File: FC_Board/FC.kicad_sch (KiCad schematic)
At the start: 82 parts, among them J1 Programmer_pins, J2 Pyro1, J3 Pyro2, J4 Pyro3, J5 Pyro4, J8 MEM2090-00-145-00-A_REVA, M1 Motor_Servo, M2 Motor_Servo, M3 Motor_Servo, M4 Motor_Servo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

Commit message: Schematic update
- Add: GPS USB and UART
- Add: USB 2.0 standard related circuitry
- Finished third SPI Bus
- Started Quad SPI Bus for data logging (SD card and Flash)
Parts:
- added BT2: Backup Bat 3.7V, Connector_JST:JST_EH_B2B-EH-A_1x02_P2.50mm_Vertical, symbol Device:Battery_Cell
- added C31, C33: 2.2uF, symbol Device:C
- added J7: USB_B_Micro, Connector_USB:USB_Micro-B_Molex-105017-0001, symbol Connector:USB_B_Micro
- added R10, R9: 27, symbol Device:R
- added R22: 100k, symbol Device:R
- added U10: ADPL44002AUJZ-5.0-R7, Package_TO_SOT_SMD:TSOT-23-5, symbol Regulator_Linear:ADP7142AUJZ-5.0
- added U11: USBLC6-2SC6, Package_TO_SOT_SMD:SOT-23-6, symbol Power_Protection:USBLC6-2SC6
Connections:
- net 3V3: no longer U7.22 (V_BCKP)
- net FLASH_EN: now also U1.57 (EBIRDY3/RPF2/SDA3/RF2)
- net GND: now also BT2.2 (-), C31.2, C33.1, J7.5 (GND), J7.6 (Shield), R22.2, U10.2 (GND), U11.2 (GND)
- net GPS_CS: now also U1.9 (EBIOE/AN19/RPC4/PMRD/RC4)
- net GPS_INT: now also U1.61 (EBIA14/PMCS1/PMA14/RA4)
- net GPS_RESET: now also U1.80 (EBID13/ETXD3/PMD13/RD13)
- net IMU_INT1: now also U1.5 (EBID7/AN15/PMD7/RE7); no longer U1.100 (EBID4/AN18/PMD4/RE4)
- net IMU_INT2: now also U1.4 (EBID6/AN16/PMD6/RE6); no longer U1.99 (EBID3/RPE3/PMD3/RE3)
- net MAG_DR: now also U1.1 (AN23/AERXERR/RG15); no longer U1.96 (TRD1/SQID1/RG12)
- net MAG_INT: now also U1.2 (EBIA5/AN34/PMA5/RA5); no longer U1.97 (TRD0/SQID0/RG13)
- net SPI3_CLK: now reaches U1.43 (EBIA1/AN9/ERXD2/AETXD3/RPB14/SCK3/PMA1/RB14)
- net SPI3_MISO: now reaches U1.47 (AN32/AETXD0/RPD14/RD14)
- net SPI3_MOSI: now reaches U1.48 (AN33/AETXD1/RPD15/SCK6/RD15)
- net at U7.5 (USB_DM): now also R10.2
- net at U7.6 (USB_DP): now also R9.2
- net VDD_USB: now reaches U7.7 (VDD_USB)
- net VDD_USB: now also C31.1, R22.1, U10.4 (SENSE/ADJ), U10.5 (VOUT)
- new net: C33.2, J7.1 (VBUS), U10.1 (VIN), U10.3 (EN), U11.5 (VBUS)
- new net: J7.2 (D-), U11.3 (I/O2)
- new net: J7.3 (D+), U11.1 (I/O1)
- new net: R9.1, U11.6 (I/O1)
- new net: R10.1, U11.4 (I/O2)
- new net V_BACKUP: BT2.1 (+), U7.22 (V_BCKP)
- no-connect marks 1 -> 4
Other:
- note added: "ESD-protection (USB2.0 standard)"
- note added: "SPI1 - MAG & IMU SPI2 - ALT/TEMP (recommended) SPI3 - GPS SPI4 - LOGGING"
- note added: "SPI3 CLK"
- note added: "SPI3 MISO"
- note added: "SPI3 MOSI"
- note added: "SPI4 CLK"
- note added: "SPI4 SIO0"
- note added: "SPI4 SIO1"
- note added: "SPI4 SIO2"
- note added: "SPI4 SIO3"
- note removed: "Adicionar interface leitura. USB maybe? Bué bulky idk..."
- note removed: "Ligar USB para dar debug ao GPS?"
- note removed: "SPI separado também. Partilhado apenas com logging"
- note removed: "SPI1 - MAG & IMU SPI2 - ALT/TEMP (sensitive/recommended) SPI3 - GPS & LOGGING"
- moved on the sheet: BT1, C11, C12, C13, C18, C19, C20, C21, C29, C3, C4, C8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

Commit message: Schematic Done
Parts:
- removed C24: 1uF, symbol Device:C_Polarized
- removed R8: 0.04, symbol Device:R_Shunt
- added C24: 1uF, Capacitor_SMD:C_0603_1608Metric_Pad1.08x0.95mm_HandSolder, symbol Device:C
- added J6: Conn_01x05, Connector_PinHeader_2.54mm:PinHeader_1x05_P2.54mm_Vertical, symbol Connector_Generic:Conn_01x05
- added R23, R24, R25, R26, R27, R28: 10k, Resistor_SMD:R_0805_2012Metric_Pad1.20x1.40mm_HandSolder, symbol Device:R
- added R29: 0.04, Resistor_SMD:R_2512_6332Metric_Pad1.40x3.35mm_HandSolder, symbol Device:R
- AE1: footprint (none) -> Connector_Coaxial:SMA_Samtec_SMA-J-P-H-ST-EM1_EdgeMount
- BT1: footprint (none) -> Connector_AMASS:AMASS_XT60IPW-M_1x03_P7.20mm_Horizontal
- BZ1: footprint (none) -> Buzzer_Beeper:Buzzer_12x9.5RM7.6; Mouser link (none) -> https://pt.mouser.com/ProductDetail/Same-Sky/CMT-1295-85T?q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
- C10, C11, C12, C13, C14, C15, C16, C9: footprint (none) -> Capacitor_SMD:C_1210_3225Metric_Pad1.33x2.70mm_HandSolder; Mouser link (none) -> https://pt.mouser.com/ProductDetail/TAIYO-YUDEN/MSASE32MSB5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
- C18: value 0.22uF -> 1uF; footprint (none) -> Capacitor_SMD:C_0603_1608Metric_Pad1.08x0.95mm_HandSolder; Mouser link (none) -> https://pt.mouser.com/ProductDetail/TAIYO-YUDEN/MLASU168SB5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
- C20: footprint (none) -> Capacitor_SMD:C_0603_1608Metric_Pad1.08x0.95mm_HandSolder; Mouser link (none) -> https://pt.mouser.com/ProductDetail/TAIYO-YUDEN/MLASU168SB5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
- C21: footprint (none) -> Capacitor_SMD:C_0805_2012Metric_Pad1.18x1.45mm_HandSolder; Mouser link (none) -> https://pt.mouser.com/ProductDetail/Murata-Electronics/GCM2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
- C31, C33: footprint (none) -> Capacitor_SMD:C_0603_1608Metric_Pad1.08x0.95mm_HandSolder; Mouser link (none) -> https://pt.mouser.com/ProductDetail/TAIYO-YUDEN/MLASE168BB7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
- D1: footprint (none) -> Diode_SMD:D_SOD-323_HandSoldering
- D2, D3: footprint (none) -> LED_THT:LED_D3.0mm
- F1: footprint (none) -> Fuse:Fuseholder_Cylinder-5x20mm_Schurter_0031_8201_Horizontal_Open; Mouser link (none) -> https://pt.mouser.com/ProductDetail/Schurter/0031.8201.G?qs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
- J1: footprint (none) -> Connector_PinHeader_2.54mm:PinHeader_1x06_P2.54mm_Horizontal
- J2, J3, J4, J5: footprint (none) -> Connector_Molex:Molex_KK-254_AE-6410-02A_1x02_P2.54mm_Vertical
- M1, M2, M3, M4: footprint (none) -> Connector_Molex:Molex_KK-254_AE-6410-03A_1x03_P2.54mm_Vertical
- Q1: footprint (none) -> Package_TO_SOT_SMD:SOT-23-3; Mouser link (none) -> https://pt.mouser.com/ProductDetail/Infineon-Technologies/B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
- Q2, Q3, Q4, Q5, Q6: footprint (none) -> Package_TO_SOT_SMD:SOT-23; Mouser link (none) -> https://pt.mouser.com/ProductDetail/Vishay-Siliconix/SQ2318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
- R10, R9: footprint (none) -> Resistor_SMD:R_0603_1608Metric_Pad0.98x0.95mm_HandSolder; Mouser link (none) -> https://pt.mouser.com/ProductDetail/Panasonic/ERJ-3RED27R0V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
- R11, R7: footprint (none) -> Resistor_SMD:R_0603_1608Metric_Pad0.98x0.95mm_HandSolder; Mouser link (none) -> https://pt.mouser.com/ProductDetail/SEI-Stackpole/RNCE0603B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
- R2: footprint (none) -> Resistor_SMD:R_0805_2012Metric_Pad1.20x1.40mm_HandSolder; Mouser link (none) -> https://pt.mouser.com/ProductDetail/Vishay/TNPW08051K00FEEA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
- R22, R3: footprint (none) -> Resistor_SMD:R_1206_3216Metric_Pad1.30x1.75mm_HandSolder; Mouser link (none) -> https://pt.mouser.com/ProductDetail/Bourns/CHV1206-JW-104EL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
- R4: footprint (none) -> Resistor_SMD:R_0805_2012Metric_Pad1.20x1.40mm_HandSolder
- U1: footprint TQFP100_PF_MCH -> QFP50P1600X1600X120-100N
- U2: footprint Package_TO_SOT_THT:TO-220-3_Vertical -> Package_TO_SOT_THT:TO-220-3_Horizontal_TabDown
- U4: footprint LSM6DS3TR-C:LGA-14-2.5X3MM -> LGA-14-2.5X3MM
- U5: footprint LIS3MDLTR:XDCR_LIS3MDLTR -> XDCR_LIS3MDLTR
- U8: footprint SOIJ8_SM_MCH -> Package_SO:SOIC-8W_5.3x5.3mm_P1.27mm; Mouser link (none) -> https://br.mouser.com/ProductDetail/Microchip-Technology/SS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
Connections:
- net 3V3: now also R4.1, C24.2, R23.2, R24.2, R25.2, R26.2, R27.2, R28.2; no longer R4.2
- net ALT_CS: now also R4.2; no longer R4.1
- net FLASH_CLK: now also J6.4 (Pin_4)
- net FLASH_EN: now also J6.1 (Pin_1)
- net GND: now also C20.2, C21.2, U3.1 (GND), C24.1, J6.5 (Pin_5)
- net Pyro1: now also U1.88 (EBID8/RPG0/PMD8/RG0); no longer U1.82 (SQICS1/RPD5/RD5)
- net SD_CMD: now also U1.82 (SQICS1/RPD5/RD5)
- net SD_D0: now also R27.1
- net SD_D1: now also R28.1
- net SD_D2: now also R25.1
- net SD_D3: now also R26.1
- net SD_IN#: now also U1.41 (EBIA11/AN7/ERXD0/AECRS/PMA11/RB12)
- net Shunt_IN: now also U9.8 (IN+), R29.1
- net Shunt_OUT: now also U9.7 (IN-), R29.2
- net FLASH_SO: now reaches U8.2 (SO/SIO1)
- net FLASH_SO: now also J6.2 (Pin_2)
- net at U8.3 (WP#/SIO2): now also R24.1
- net FLASH_SI: now reaches U8.5 (SI/SIO0)
- net FLASH_SI: now also J6.3 (Pin_3)
- net at U8.7 (HOLD/SIO3): now also R23.1
- net SPI4_CLK: now reaches U1.89 (TRCLK/SQICLK/RA6)
- net SPI4_SIO3: now reaches U1.90 (TRD3/SQID3/RA7)
- net SPI4_SIO2: now reaches U1.95 (TRD2/SQID2/RG14)
- net SPI4_SIO1: now reaches U1.96 (TRD1/SQID1/RG12)
- net SPI4_SIO0: now reaches U1.97 (TRD0/SQID0/RG13)
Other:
- note added: "Conector para leitura externa"
- note added: "FLASH DATA LOGGING"
- note added: "SPI1 - MAG & IMU SPI2 - ALT/TEMP (recommended) SPI3 - GPS & FLASH SPI4 - SD CARD"
- note added: "Zener dá clamp para cumprir máx vgs quando reverse polarity. Para o PMOS que escolhi não é necessário."
- note removed: "Como é que este CMD funciona? Sequer preciso em modo SPI?"
- note removed: "GPS FLASH DATA LOGGING"
- note removed: "SPI1 - MAG & IMU SPI2 - ALT/TEMP (recommended) SPI3 - GPS SPI4 - LOGGING"
- note removed: "Zener dá clamp para cumprir máx vgs quando reverse polarity"
- moved on the sheet: C21, U3

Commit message: Started PCB
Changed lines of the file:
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@@
-	)
-	(junction
-		(at 208.28 102.87)
-		(diameter 0)
-		(color 0 0 0 0)
 	)
 	(junction
@@
 	(junction
 		(at 262.89 256.54)
-		(diameter 0)
-		(color 0 0 0 0)
-	)
-	(junction
-		(at 208.28 67.31)
 		(diameter 0)
 		(color 0 0 0 0)
@@
 		)
 		(stroke
-			(width 0)
-			(type default)
-		)
-	)
-	(wire
-		(pts
-			(xy 208.28 67.31) (xy 208.28 102.87)
-		)
-		(stroke

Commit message: First placement attempt
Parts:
- BT1: footprint Connector_AMASS:AMASS_XT60IPW-M_1x03_P7.20mm_Horizontal -> Connector_AMASS:AMASS_XT60-M_1x02_P7.20mm_Vertical
- U2: footprint Package_TO_SOT_THT:TO-220-3_Horizontal_TabDown -> Package_TO_SOT_THT:TO-220-3_Vertical
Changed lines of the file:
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@@
 			)
 		)
-		(property "Footprint" "Package_TO_SOT_THT:TO-220-3_Horizontal_TabDown"
+		(property "Footprint" "Package_TO_SOT_THT:TO-220-3_Vertical"
 			(at 91.44 50.165 0)
 			(effects
@@
 			)
 		)
-		(property "Footprint" "Connector_AMASS:AMASS_XT60IPW-M_1x03_P7.20mm_Horizontal"
+		(property "Footprint" "Connector_AMASS:AMASS_XT60-M_1x02_P7.20mm_Vertical"
 			(at 30.48 63.246 90)
 			(effects

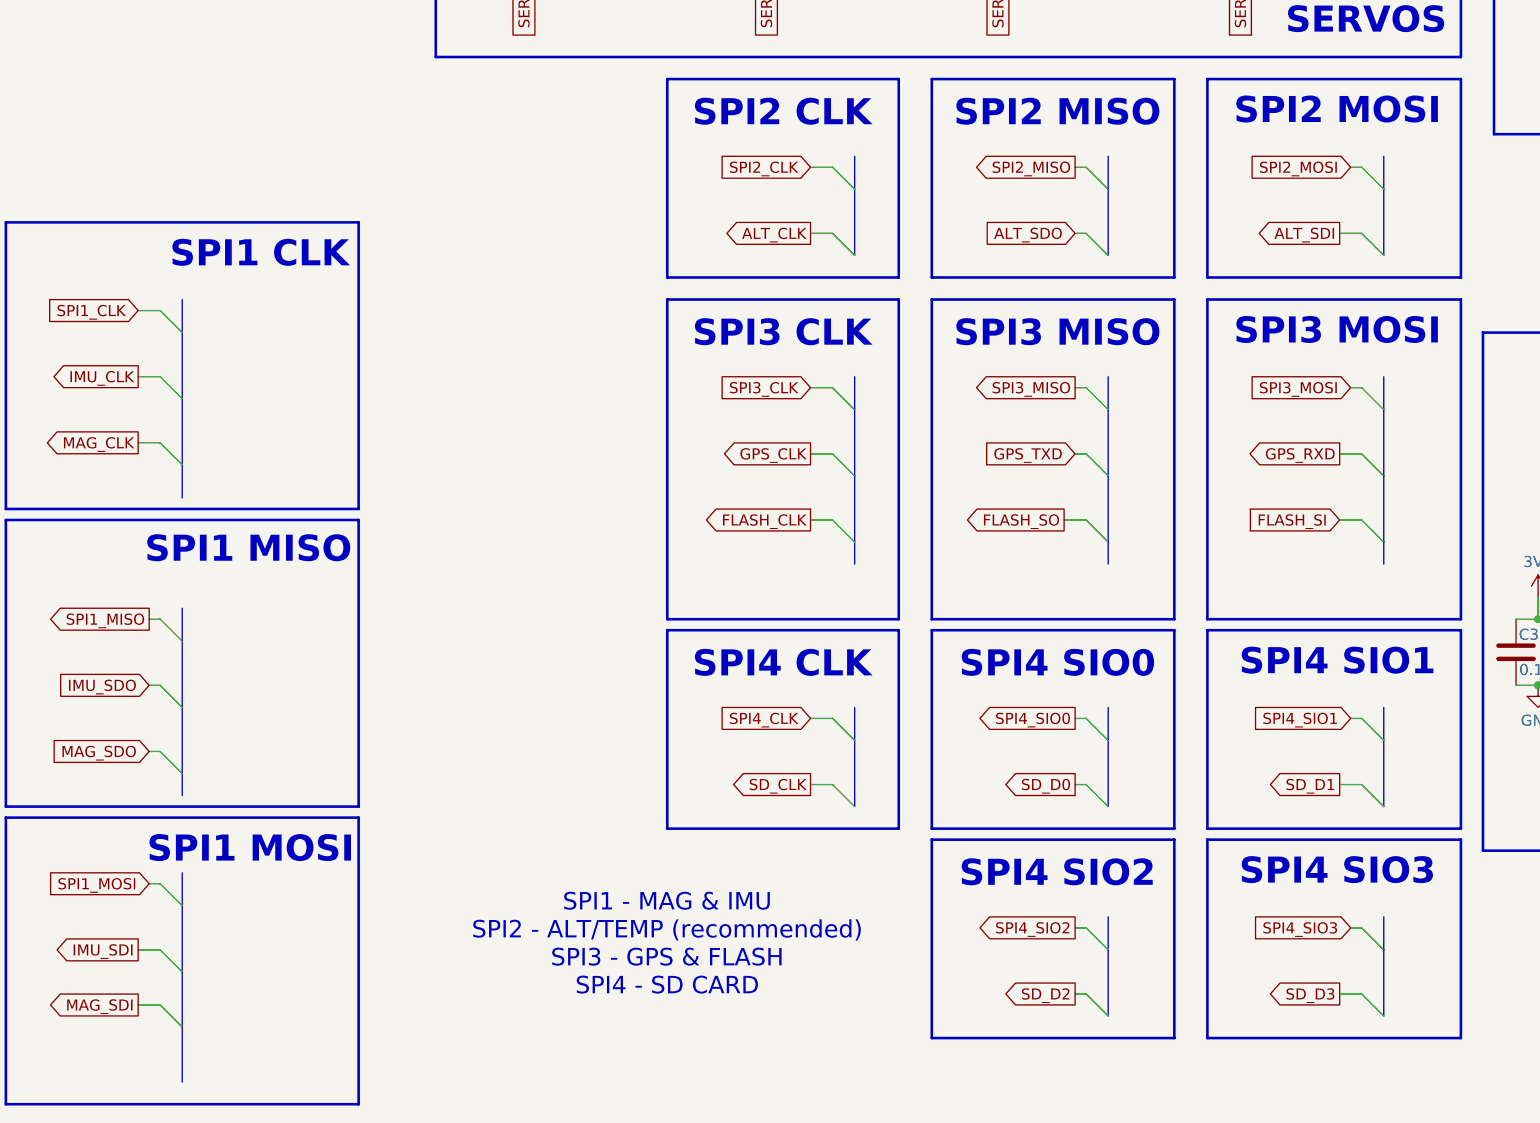
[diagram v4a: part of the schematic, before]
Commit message: Transitioning to 4 layers
Tried 2 layer routing to minimize cost. Too many tracks...
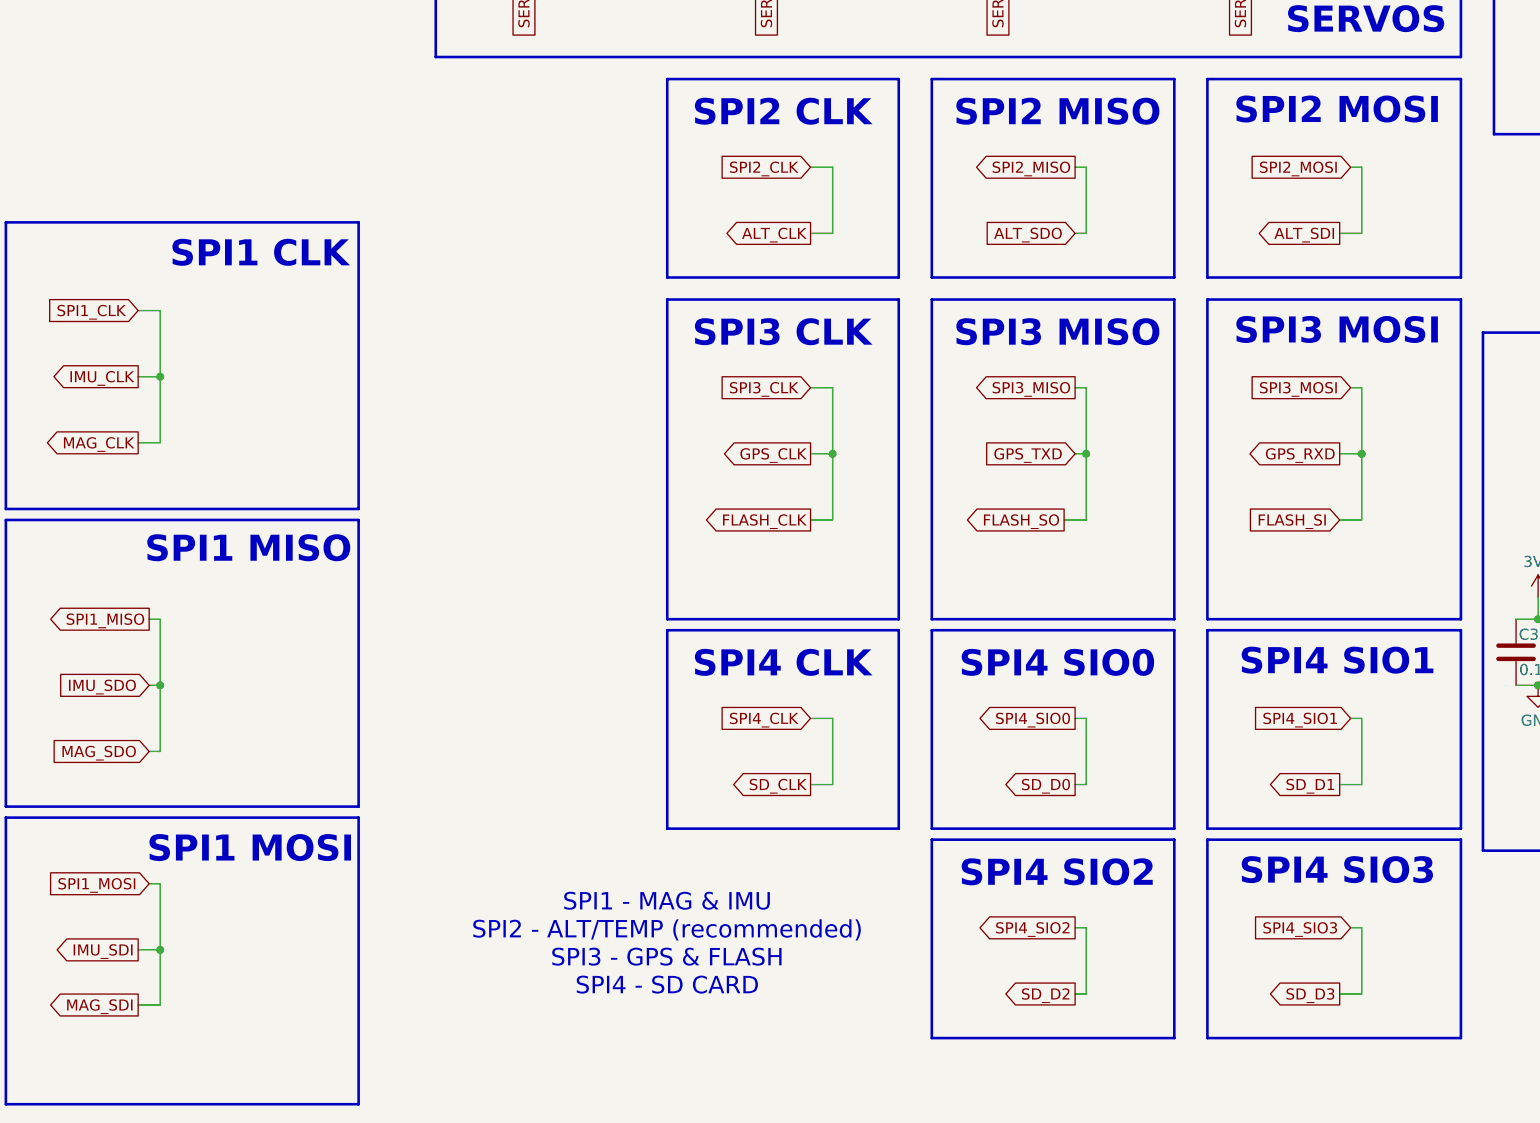
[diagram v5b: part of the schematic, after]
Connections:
- net GPS_CLK is gone; now on net FLASH_CLK: U7.19 (SCL/SPI_CLK)
- net GPS_RXD is gone; now on net FLASH_SI: U7.21 (RXD/SPI_MOSI)
- net GPS_TXD is gone; now on net FLASH_SO: U7.20 (TXD/SPI_MISO)
- net MAG_CLK is gone; now on net IMU_CLK: U5.1 (SCL/SPC)
- net MAG_SDI is gone; now on net IMU_SDI: U5.11 (SDA/SDI/SDO)
- net MAG_SDO is gone; now on net IMU_SDO: U5.9 (SDO/SA1)
- net SPI1_CLK is gone; now on net IMU_CLK: U1.76 (RPD1/SCK1/RD1)
- net SPI1_MISO is gone; now on net IMU_SDO: U1.73 (SOSCO/RPC14/T1CK/RC14)
- net SPI1_MOSI is gone; now on net IMU_SDI: U1.72 (SOSCI/RPC13/RC13)
- net SPI2_CLK is gone; now on net ALT_CLK: U1.10 (AN14/C1IND/ECOL/RPG6/SCK2/RG6)
- net SPI2_MISO is gone; now on net ALT_SDO: U1.6 (EBIA6/AN22/RPC1/PMA6/RC1)
- net SPI2_MOSI is gone; now on net ALT_SDI: U1.7 (EBIA12/AN21/RPC2/PMA12/RC2)
- net SPI3_CLK is gone; now on net FLASH_CLK: U1.43 (EBIA1/AN9/ERXD2/AETXD3/RPB14/SCK3/PMA1/RB14)
- net SPI3_MISO is gone; now on net FLASH_SO: U1.47 (AN32/AETXD0/RPD14/RD14)
- net SPI3_MOSI is gone; now on net FLASH_SI: U1.48 (AN33/AETXD1/RPD15/SCK6/RD15)
- net SPI4_CLK is gone; now on net SD_CLK: U1.89 (TRCLK/SQICLK/RA6)
- net SPI4_SIO0 is gone; now on net SD_D0: U1.97 (TRD0/SQID0/RG13)
- net SPI4_SIO1 is gone; now on net SD_D1: U1.96 (TRD1/SQID1/RG12)
- net SPI4_SIO2 is gone; now on net SD_D2: U1.95 (TRD2/SQID2/RG14)
- net SPI4_SIO3 is gone; now on net SD_D3: U1.90 (TRD3/SQID3/RA7)
